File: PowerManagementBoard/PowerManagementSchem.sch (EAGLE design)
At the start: 100 parts, among them J1 D15S24A4GV00LF, J2 455-1750-1-ND, U1 VX7805-500, U2 PYB20-Q24-S5, U3 PYB30-Q48-S5, U4 PYB30-Q48-S12, U5 3V3REG, U6 INA4180-SPLIT, U7 INA4180-SPLIT, U8 TEENSY-4.0SILK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

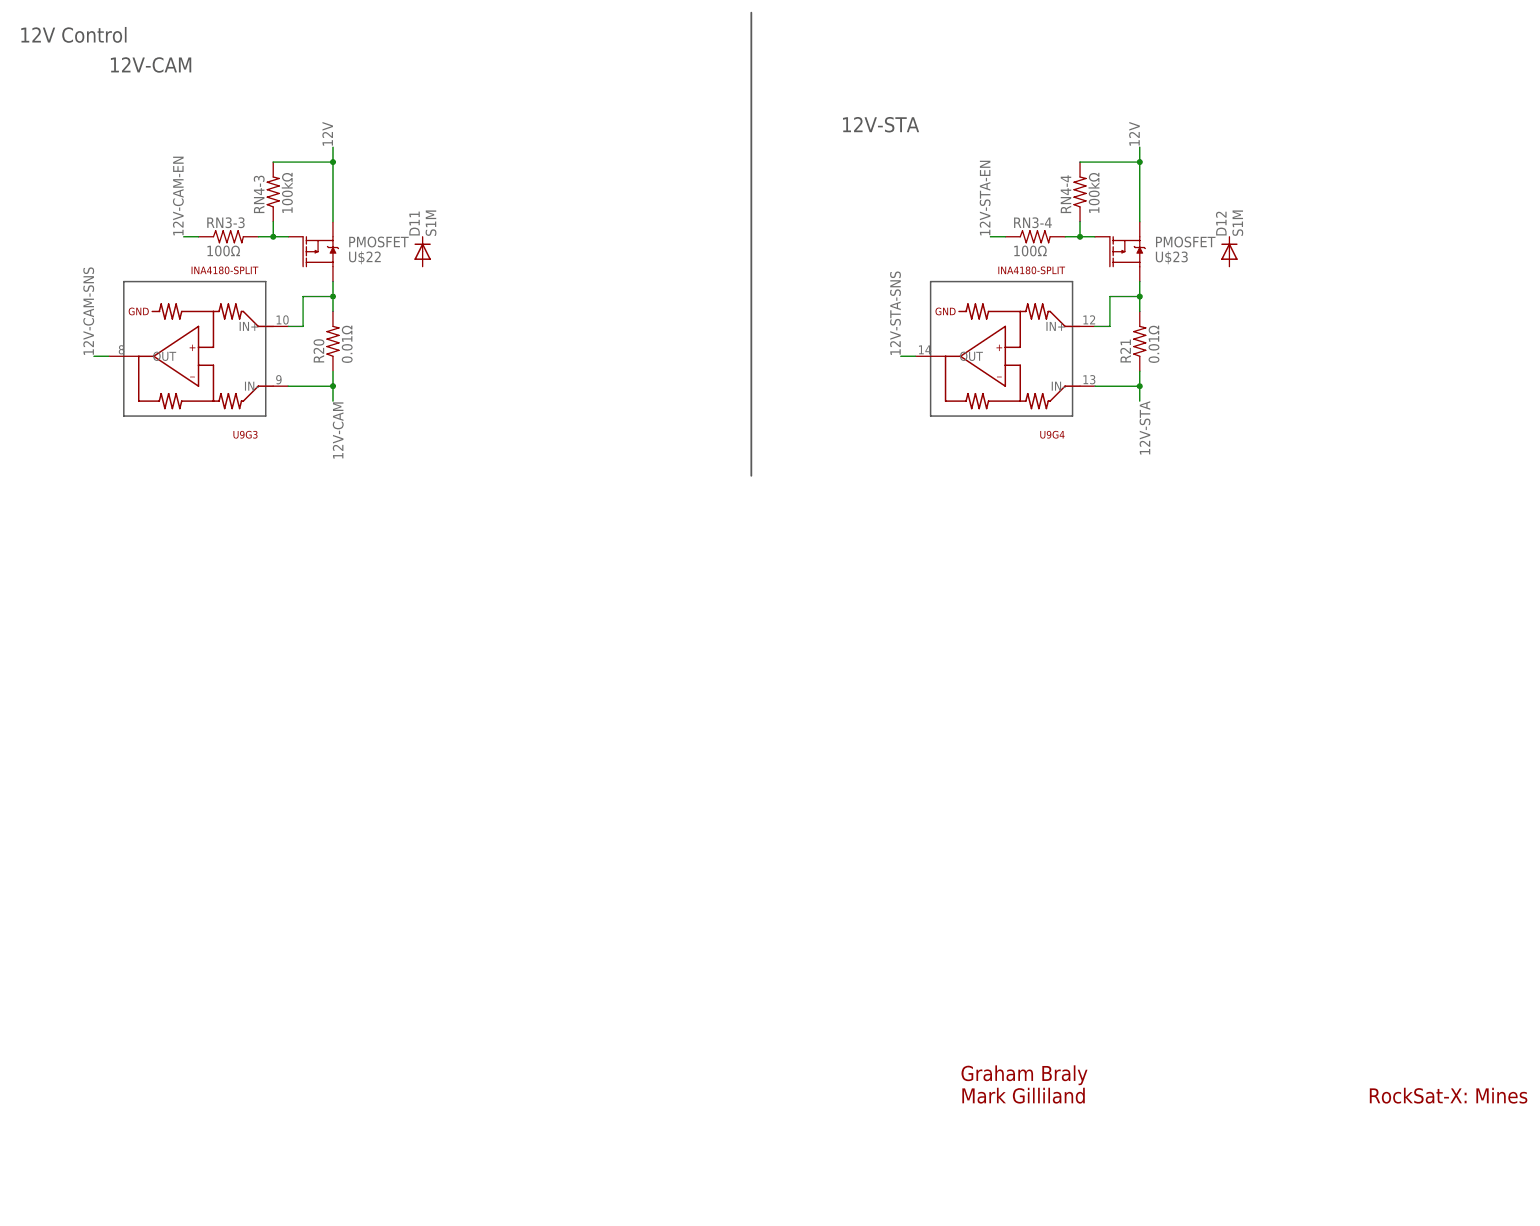
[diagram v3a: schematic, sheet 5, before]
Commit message: added db 37 and db25
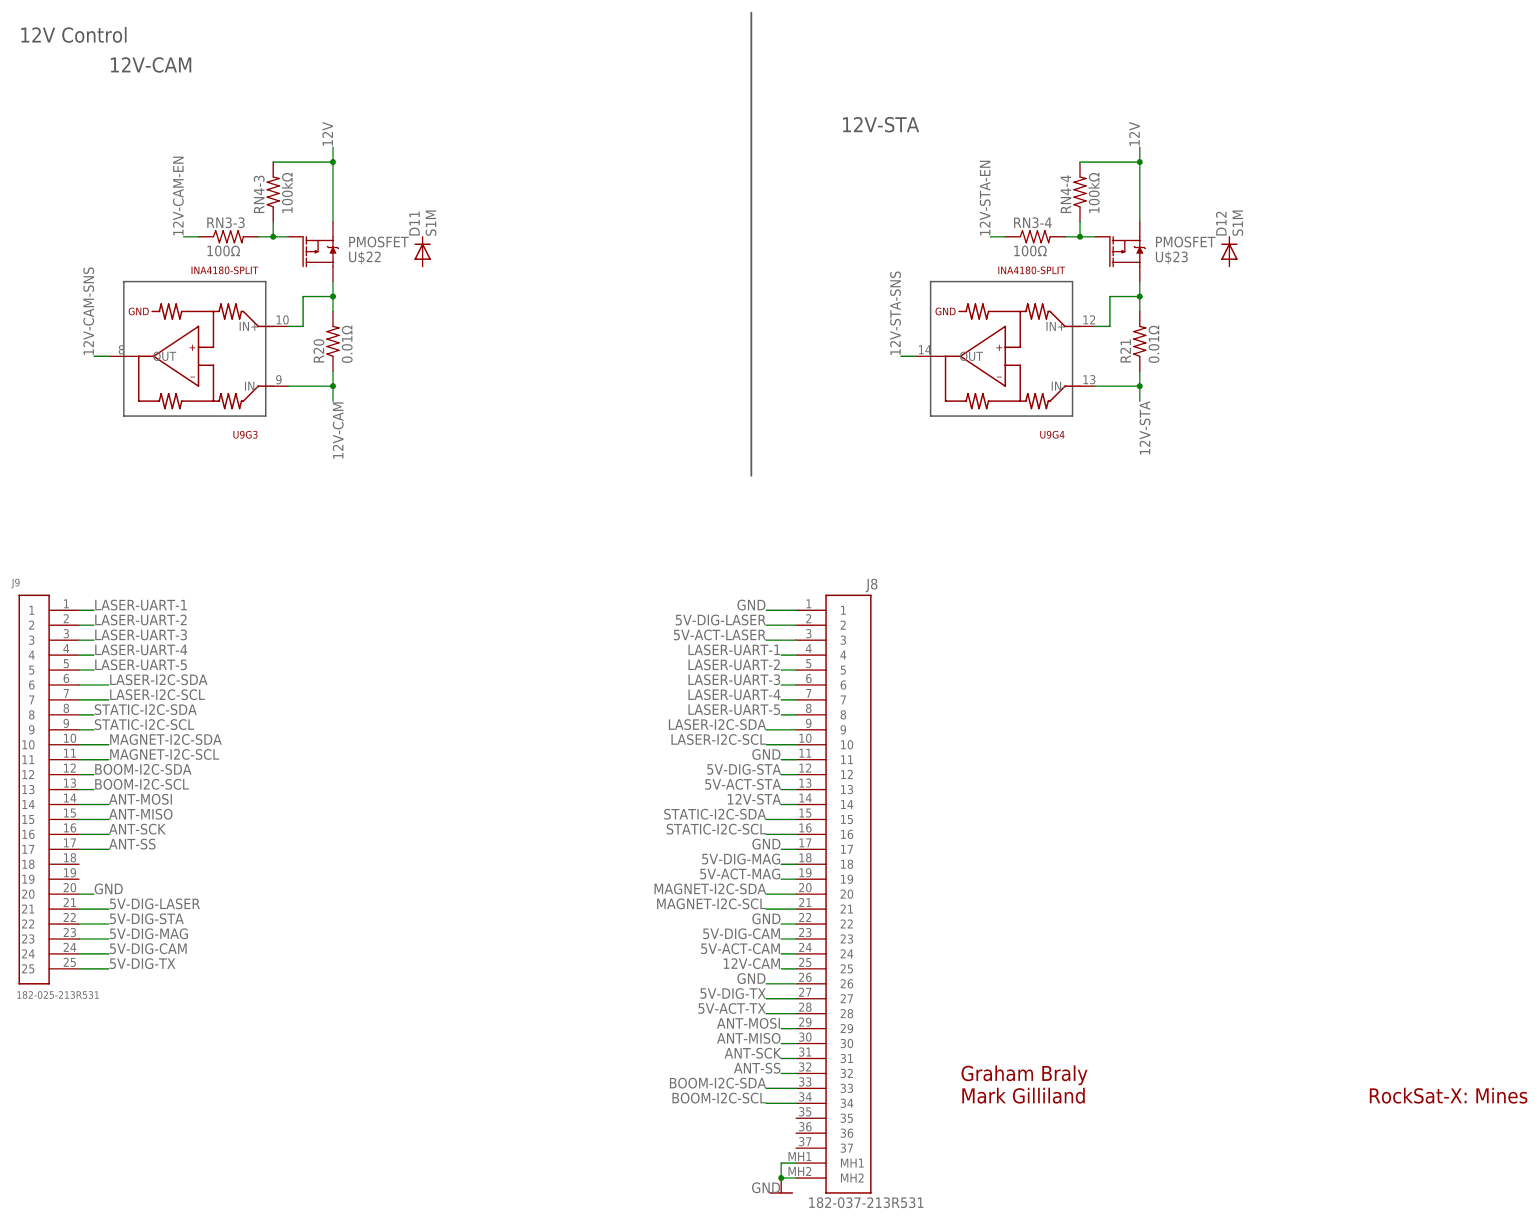
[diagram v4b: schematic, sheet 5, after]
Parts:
- added J8: 182-037-213R531, D-Sub Connectors:182-037-213R531
- added J9: 182-025-213R531, D-Sub Connectors:182-025-213R531
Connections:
- new net ANT-MISO: J8.30, J9.15
- new net ANT-MOSI: J8.29, J9.14
- new net ANT-SCK: J8.31, J9.16
- new net ANT-SS: J8.32, J9.17
- new net BOOM-I2C-SCL: J8.34, J9.13
- new net BOOM-I2C-SDA: J8.33, J9.12
- new net LASER-I2C-SCL: J8.10, J9.7
- new net LASER-I2C-SDA: J8.9, J9.6
- new net LASER-UART-1: J8.4, J9.1
- new net LASER-UART-2: J8.5, J9.2
- new net LASER-UART-3: J8.6, J9.3
- new net LASER-UART-4: J8.7, J9.4
- new net LASER-UART-5: J8.8, J9.5
- new net MAGNET-I2C-SCL: J8.21, J9.11
- new net MAGNET-I2C-SDA: J8.20, J9.10
- new net STATIC-I2C-SCL: J8.16, J9.9
- new net STATIC-I2C-SDA: J8.15, J9.8
- net 12V-CAM: now also J8.25
- net 12V-STA: now also J8.14
- net 5V-ACT-CAM: now also J8.24
- net 5V-ACT-LASER: now also J8.3
- net 5V-ACT-MAG: now also J8.19
- net 5V-ACT-STA: now also J8.13
- net 5V-ACT-TX: now also J8.28
- net 5V-DIG-CAM: now also J8.23, J9.24
- net 5V-DIG-LASER: now also J8.2, J9.21
- net 5V-DIG-MAG: now also J8.18, J9.23
- net 5V-DIG-STA: now also J8.12, J9.22
- net 5V-DIG-TX: now also J8.27, J9.25
- net GND: now also J8.1, J8.11, J8.17, J8.22, J8.26, J8.MH1, J8.MH2, J9.20

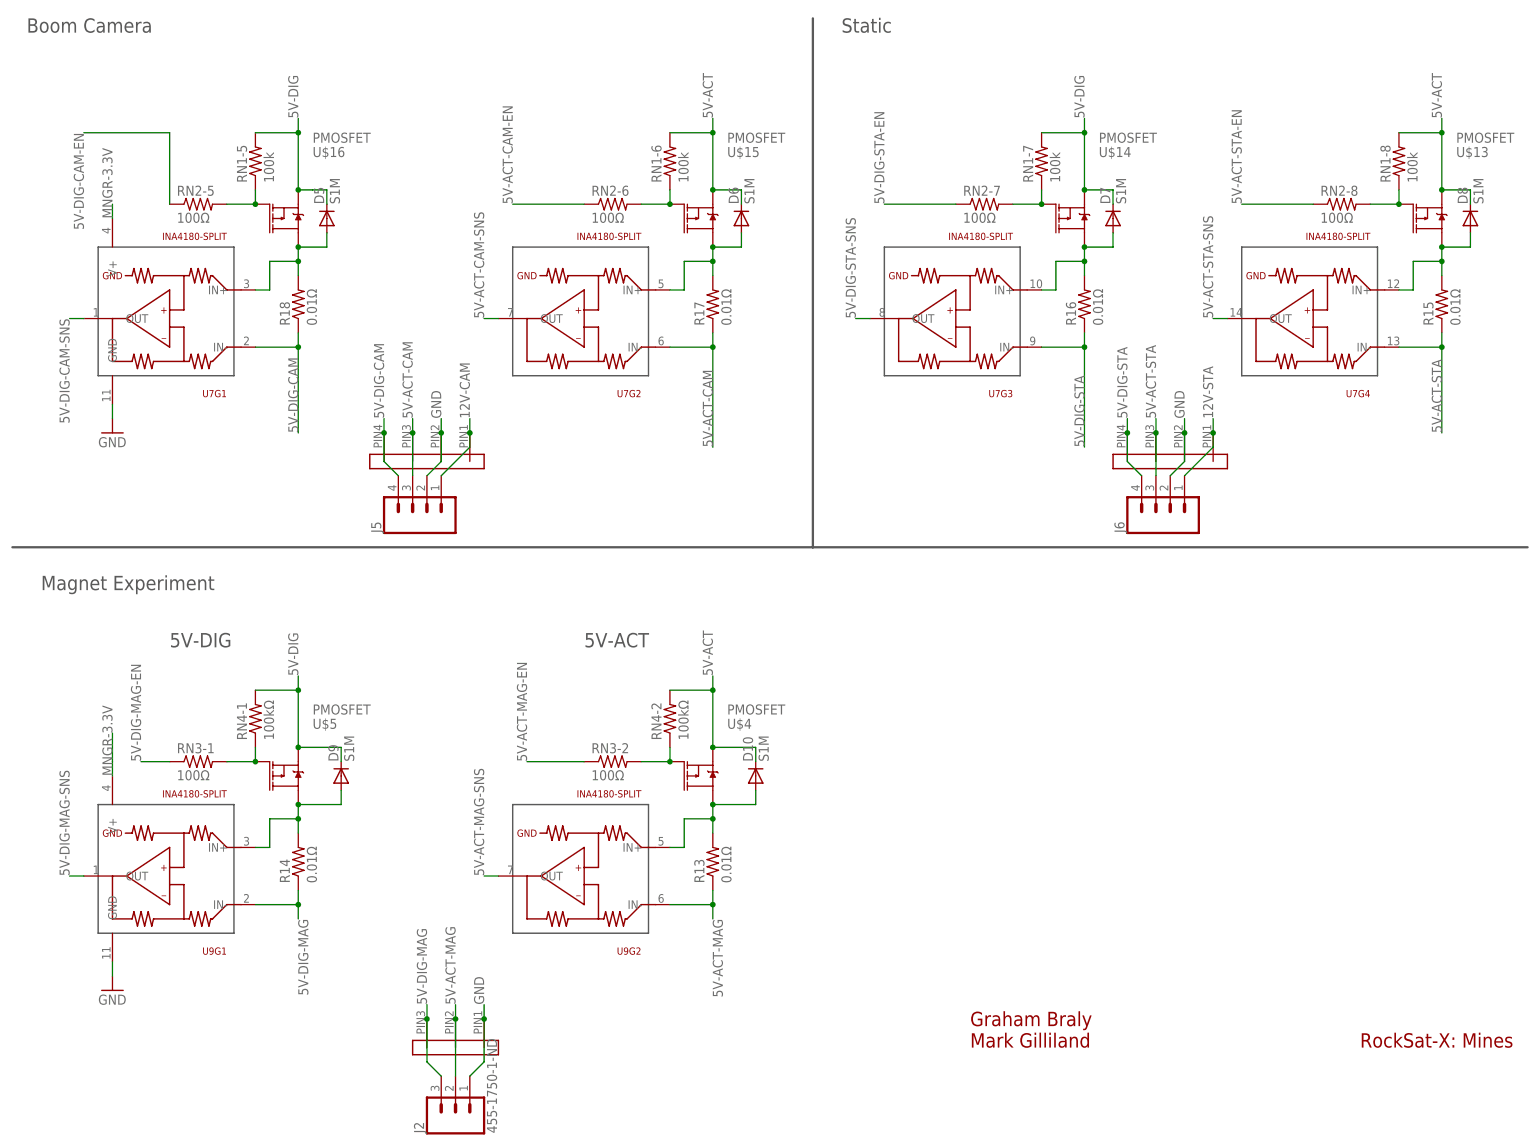
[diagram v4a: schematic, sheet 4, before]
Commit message: Power Board: Removed molex connectors, started routing signals
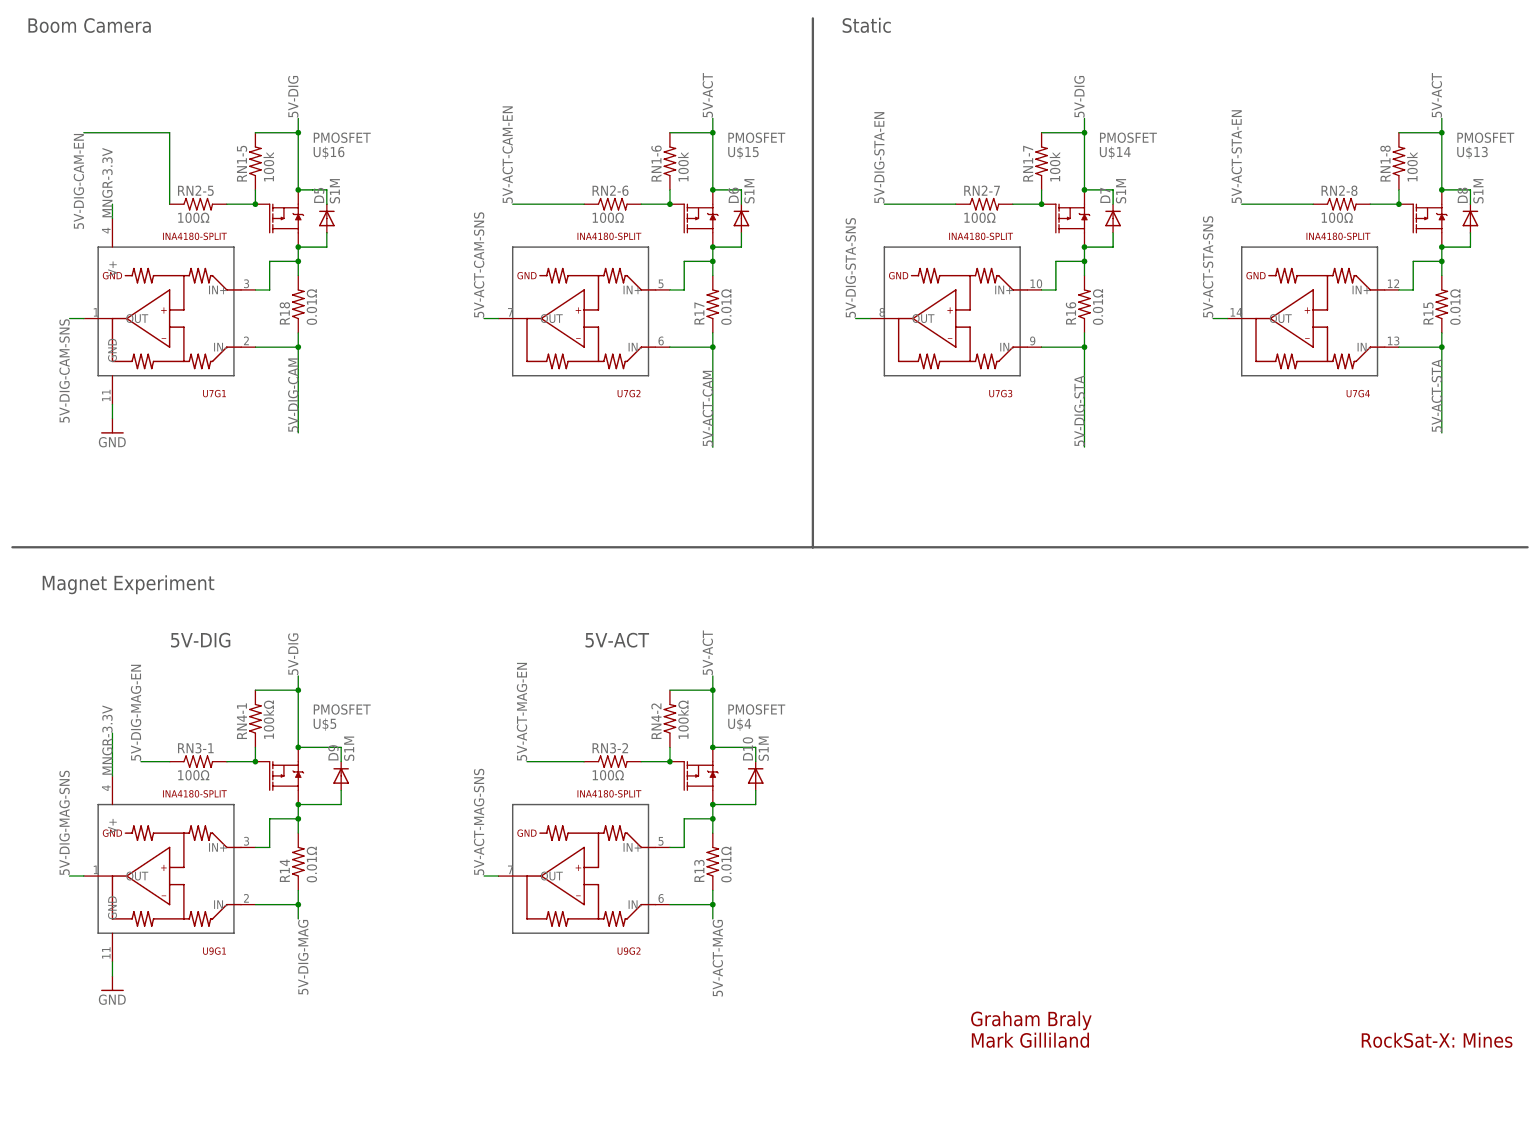
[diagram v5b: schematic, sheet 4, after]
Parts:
- removed J2: 455-1750-1-ND, SparkFun-Connectors:CONN_03
- removed J3, J4: (no value), SparkFun-Connectors:CONN_03
- removed J5, J6: (no value), SparkFun-Connectors:CONN_04PTH
- removed U$11, U$12: MOLEX_4PIN, PowerManagementParts:MOLEX_4PIN
- removed U$2, U$24, U$3: MOLEX_3PIN, PowerManagementParts:MOLEX_3PIN
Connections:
- net 12V: now also D11.C, D12.C
- net 12V-CAM: no longer J5.1, U$11.PIN1
- net 12V-STA: no longer J6.1, U$12.PIN1
- net 5V-ACT-CAM: no longer J5.3, U$11.PIN3
- net 5V-ACT-LASER: no longer J4.2, U$3.PIN2
- net 5V-ACT-MAG: no longer J2.2, U$24.PIN2
- net 5V-ACT-STA: no longer J6.3, U$12.PIN3
- net 5V-ACT-TX: no longer J3.2, U$2.PIN2
- net 5V-DIG: now also D1.C
- net 5V-DIG-CAM: no longer J5.4, U$11.PIN4
- net 5V-DIG-LASER: no longer J4.3, U$3.PIN3
- net 5V-DIG-MAG: no longer J2.3, U$24.PIN3
- net 5V-DIG-STA: no longer J6.4, U$12.PIN4
- net 5V-DIG-TX: no longer J3.3, U$2.PIN3
- net GND: no longer J2.1, J3.1, J4.1, J5.2, J6.2, U$11.PIN2, U$12.PIN2, U$2.PIN1, U$24.PIN1, U$3.PIN1
- net N$11: now also D1.A
- net N$34: now also D11.A
- net N$36: now also D12.A

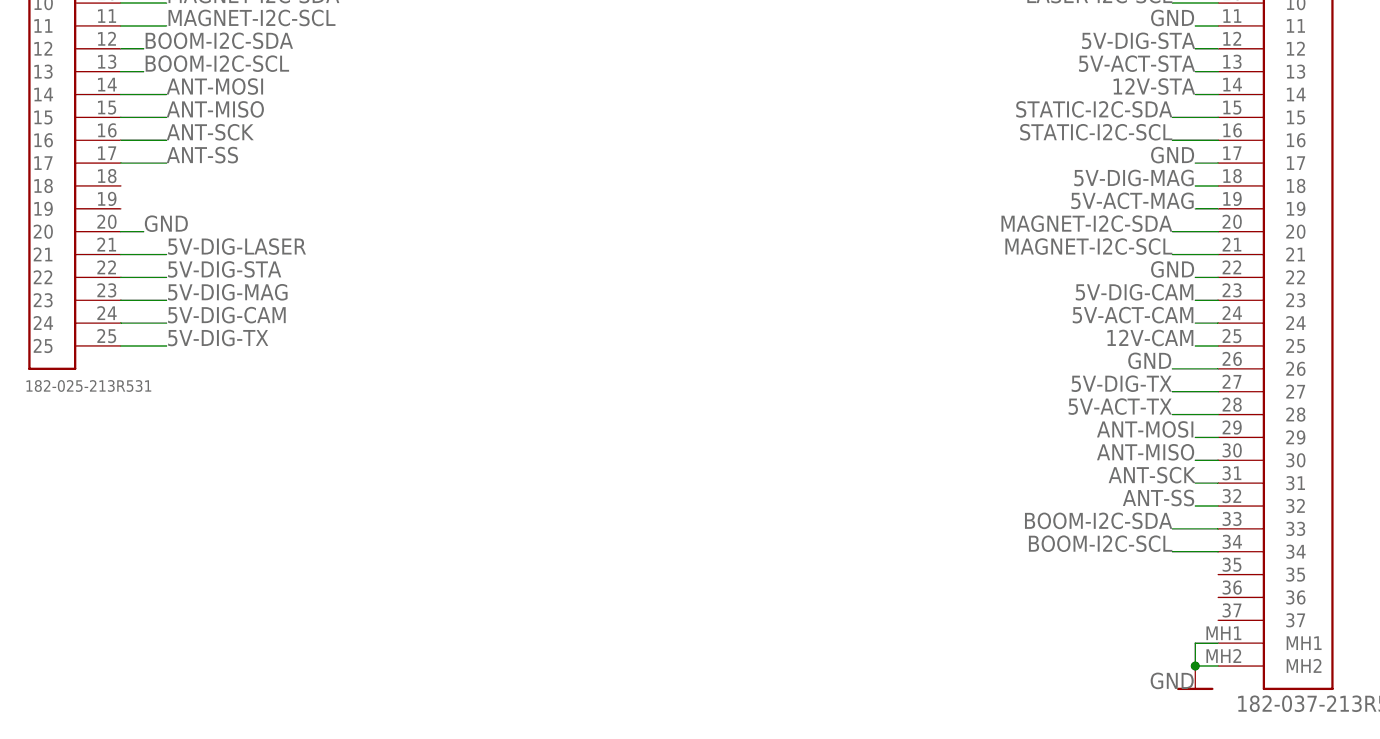
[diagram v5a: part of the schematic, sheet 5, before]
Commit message: Added USB lines for the camera
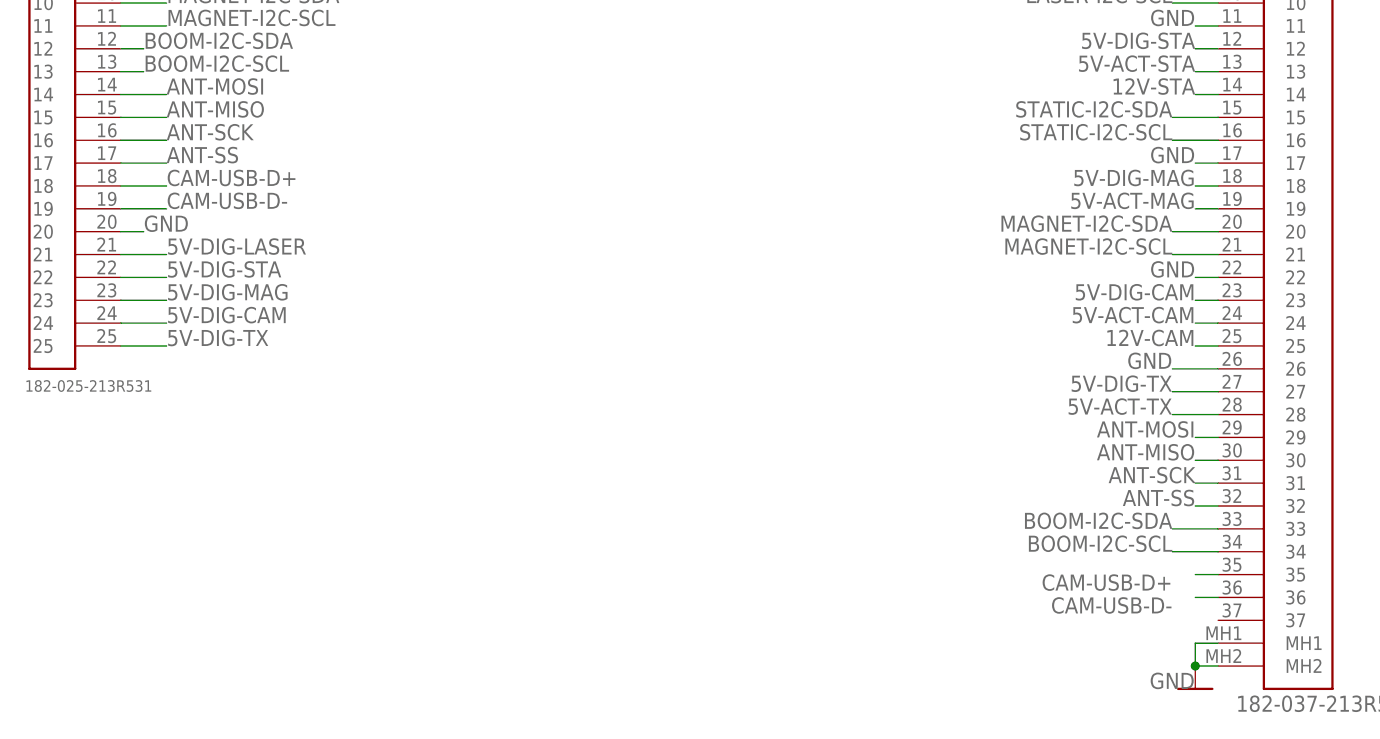
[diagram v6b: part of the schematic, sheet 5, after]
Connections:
- new net CAM-USB-D+: J8.35, J9.18
- new net CAM-USB-D-: J8.36, J9.19
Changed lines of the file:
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@@
 <?xml version="1.0" encoding="utf-8"?>
 <!DOCTYPE eagle SYSTEM "eagle.dtd">
-<eagle version="9.5.2">
+<eagle version="9.4.2">
 <drawing>
 <settings>
@@
 </segment>
 </net>
+<net name="CAM-USB-D+" class="0">
+<segment>
+<pinref part="J9" gate="G$1" pin="18"/>
+<wire x1="25.4" y1="66.04" x2="30.48" y2="66.04" width="0.1524" layer="91"/>
+<label x="30.48" y="66.04" size="1.778" layer="95"/>
+</segment>
+<segment>
+<pinref part="J8" gate="G$1" pin="35"/>
+<wire x1="147.32" y1="22.86" x2="144.78" y2="22.86" width="0.1524" layer="91"/>
+<label x="142.24" y="22.86" size="1.778" layer="95" rot="R180"/>
+</segment>
+</net>
+<net name="CAM-USB-D-" class="0">
+<segment>
+<pinref part="J8" gate="G$1" pin="36"/>
+<wire x1="147.32" y1="20.32" x2="144.78" y2="20.32" width="0.1524" layer="91"/>
+<label x="142.24" y="20.32" size="1.778" layer="95" rot="R180"/>
+</segment>
+<segment>
+<pinref part="J9" gate="G$1" pin="19"/>
+<wire x1="25.4" y1="63.5" x2="30.48" y2="63.5" width="0.1524" layer="91"/>
+<label x="30.48" y="63.5" size="1.778" layer="95"/>
+</segment>
+</net>
